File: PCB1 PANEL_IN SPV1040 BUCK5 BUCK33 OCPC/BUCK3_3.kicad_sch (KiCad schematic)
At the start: 0 parts

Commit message: 2
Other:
- company: (none) -> TEAM ANANT
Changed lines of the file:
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@@
 	(generator_version "8.0")
 	(paper "A4")
+	(title_block
+		(company "TEAM ANANT")
+		(comment 1 "BITS PILANI")
+	)
 	(global_label "VBUS_IN"
 		(shape bidirectional)

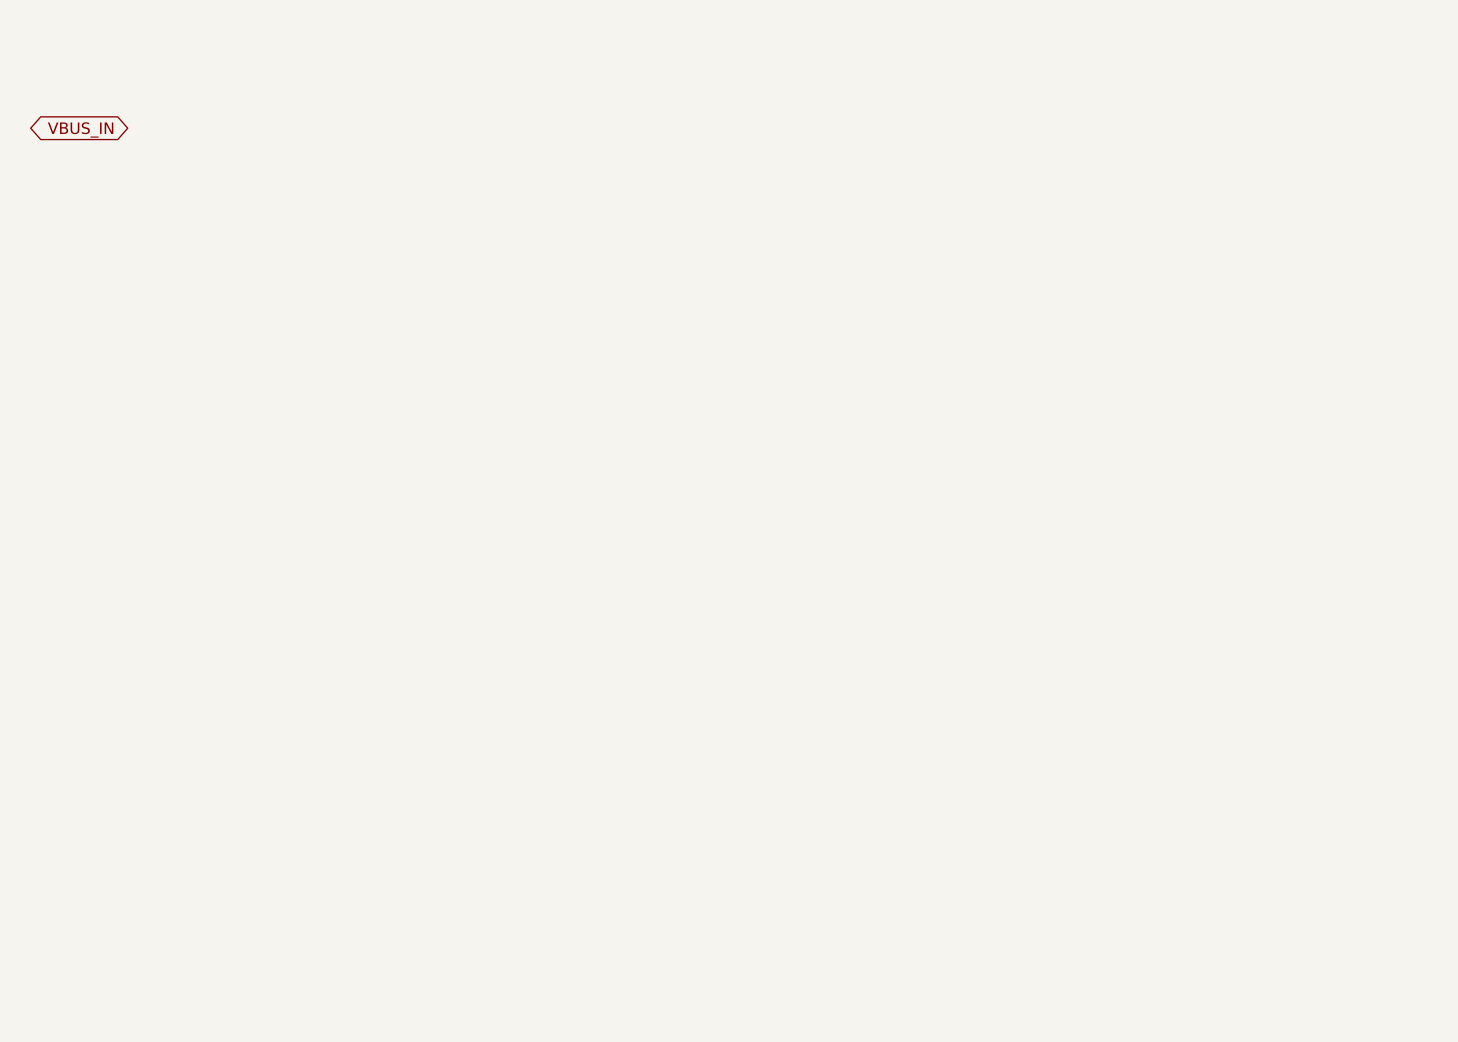
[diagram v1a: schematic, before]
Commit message: Changes
Added bucks from old work
and copied SPV
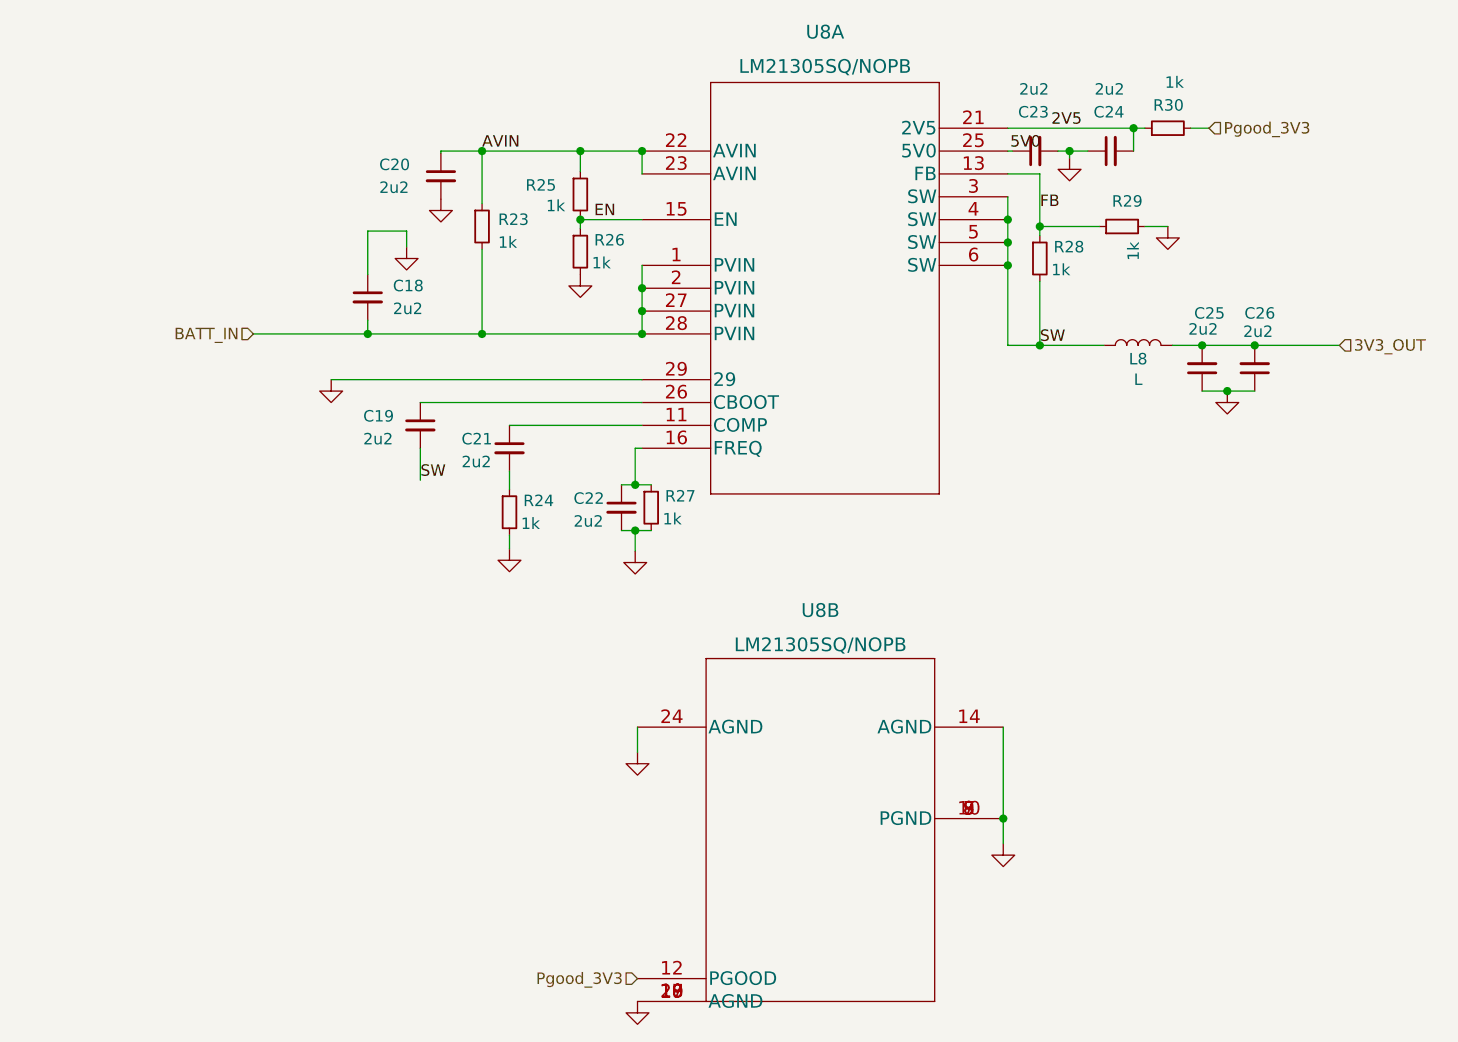
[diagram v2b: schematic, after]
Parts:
- added C18: 2u2, Capacitor_Tantalum_SMD:CP_EIA-7343-43_Kemet-X_Pad2.25x2.55mm_HandSolder, symbol Device:C_Small
- added C19, C20, C21, C22, C23, C24, C25, C26: 2u2, Capacitor_SMD:C_0603_1608Metric_Pad1.08x0.95mm_HandSolder, symbol Device:C_Small
- added L8: L, Inductor_SMD:L_6.3x6.3_H3, symbol Device:L
- added R23, R24, R25, R26, R27, R28, R29, R30: 1k, Resistor_SMD:R_0603_1608Metric_Pad0.98x0.95mm_HandSolder, symbol Device:R_Small
- added U8: LM21305SQ/NOPB, footprintLM21305:LM21305SQ&slash_NOPB, symbol 2023-03-29_16-01-02:LM21305SQ/NOPB
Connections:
- new net: C19.1, U8.26 (CBOOT)
- new net: C22.1, R27.1, U8.16 (FREQ)
- new net: C21.2, R24.1
- new net: C21.1, U8.11 (COMP)
- new net 2V5: C24.2, R30.1, U8.21 (2V5)
- new net 3V3_OUT: C25.2, C26.2, L8.2
- new net 5V0: C23.1, U8.25 (5V0)
- new net AVIN: C20.1, R23.1, R25.1, U8.22 (AVIN), U8.23 (AVIN)
- new net BATT_IN: C18.2, R23.2, U8.1 (PVIN), U8.2 (PVIN), U8.27 (PVIN), U8.28 (PVIN)
- new net EN: R25.2, R26.1, U8.15 (EN)
- new net FB: R28.1, R29.1, U8.13 (FB)
- new net GND: C18.1, C20.2, C22.2, C23.2, C24.1, C25.1, C26.1, R24.2, R26.2, R27.2, R29.2, U8.10 (PGND), U8.14 (AGND), U8.17 (AGND), U8.18 (AGND), U8.19 (AGND), U8.20 (AGND), U8.24 (AGND), U8.29, U8.7 (PGND), U8.8 (PGND), U8.9 (PGND)
- new net Pgood_3V3: R30.2, U8.12 (PGOOD)
- new net SW: C19.2, L8.1, R28.2, U8.3 (SW), U8.4 (SW), U8.5 (SW), U8.6 (SW)
